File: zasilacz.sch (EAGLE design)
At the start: 26 parts, among them IC2 7812TV

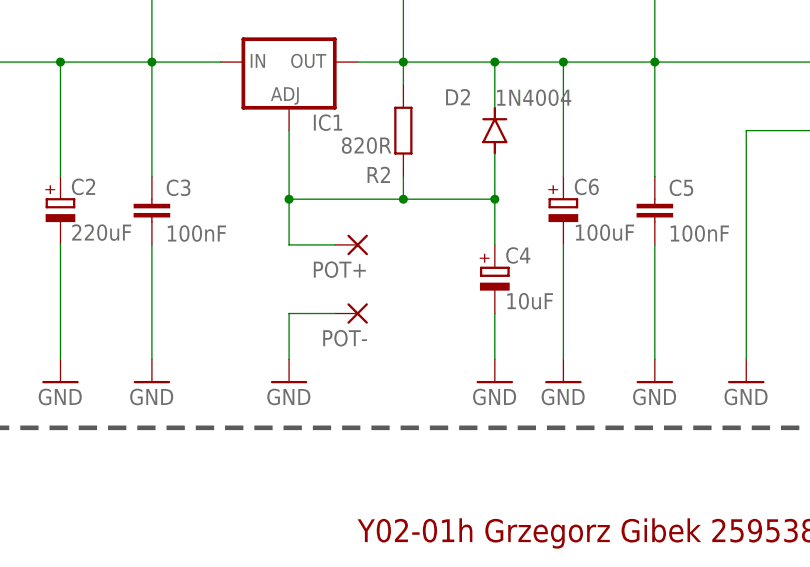
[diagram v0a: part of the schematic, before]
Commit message: Dodanie wartości potencjometru
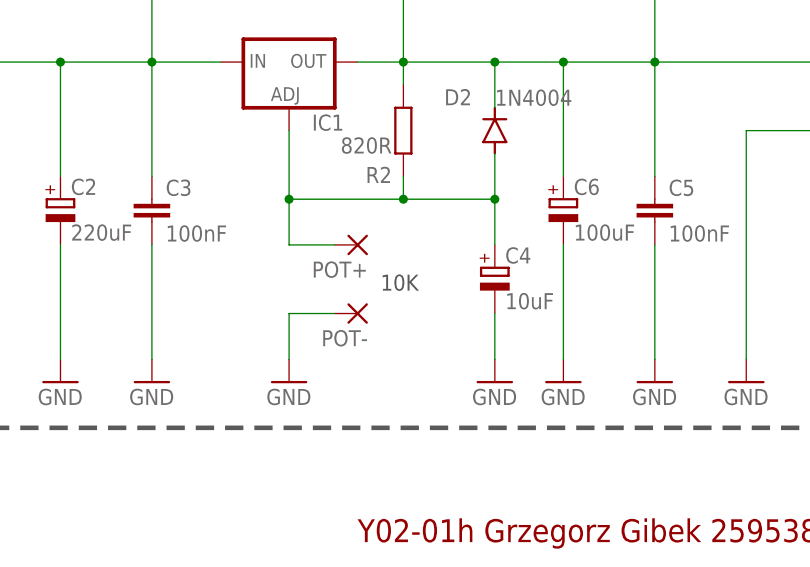
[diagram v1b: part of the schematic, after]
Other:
- note added: "10K"
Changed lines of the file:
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@@
 <wire x1="152.4" y1="157.48" x2="152.4" y2="109.22" width="0.508" layer="97" style="shortdash"/>
 <text x="160.02" y="152.4" size="3.81" layer="97">ZASILANIE WOLTOMIERZA</text>
+<text x="170.18" y="55.88" size="1.778" layer="97">10K</text>
 </plain>
 <instances>
